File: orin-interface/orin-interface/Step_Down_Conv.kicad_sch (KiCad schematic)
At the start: 2 parts, among them U1 173950336

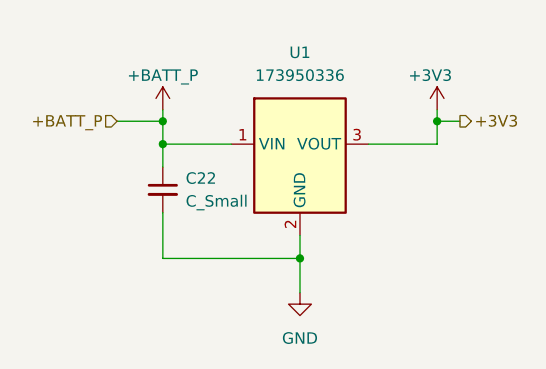
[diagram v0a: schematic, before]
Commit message: orin-interface: PoE channels, buses, 3V3 regulator, ERC fixes
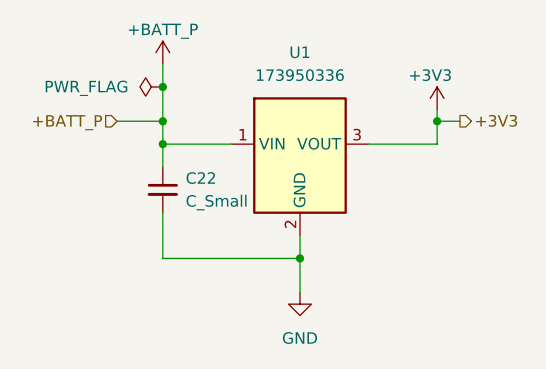
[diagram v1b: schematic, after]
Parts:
- C22: footprint (none) -> Capacitor_SMD:C_0603_1608Metric_Pad1.08x0.95mm_HandSolder
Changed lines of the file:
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@@
+	)
+	(junction
+		(at 134.62 77.47)
+		(diameter 0)
+		(color 0 0 0 0)
 	)
 	(junction
@@
 	(wire
 		(pts
+			(xy 134.62 77.47) (xy 134.62 81.28)
+		)
+		(stroke
+			(width 0)
+			(type default)
+		)
+	)
+	(wire
+		(pts
 			(xy 134.62 83.82) (xy 142.24 83.82)
 		)
@@
 	(wire
 		(pts
-			(xy 134.62 80.01) (xy 134.62 81.28)
+			(xy 134.62 74.93) (xy 134.62 77.47)
 		)
 		(stroke
@@
 	)
 	(symbol
+		(lib_id "power:PWR_FLAG")
+		(at 134.62 77.47 90)
+		(unit 1)
+		(body_style 1)
+		(exclude_from_sim no)
+		(in_bom yes)
+		(on_board yes)
+		(in_pos_files yes)
+		(dnp no)
+		(fields_autoplaced yes)
+		(property "Reference" "#FLG02"
+			(at 132.715 77.47 0)
+			(hide yes)
+			(show_name no)
+			(do_not_autoplace no)
+			(effects
+				(font
+					(size 1.27 1.27)
+				)
+			)
+		)
+		(property "Value" "PWR_FLAG"
+			(at 130.81 77.4699 90)
+			(show_name no)
+			(do_not_autoplace no)
+			(effects
+				(font
+					(size 1.27 1.27)
+				)
+				(justify left)
+			)
+		)
+		(property "Footprint" ""
+			(at 134.62 77.47 0)
+			(hide yes)
+			(show_name no)
+			(do_not_autoplace no)
+			(effects
+				(font
+					(size 1.27 1.27)
+				)
+			)
+		)
+		(property "Datasheet" ""
+			(at 134.62 77.47 0)
+			(hide yes)
+			(show_name no)
+			(do_not_autoplace no)
+			(effects
+				(font
+					(size 1.27 1.27)
+				)
+			)
+		)
+		(property "Description" "Special symbol for telling ERC where power comes from"
+			(at 134.62 77.47 0)
+			(hide yes)
+			(show_name no)
+			(do_not_autoplace no)
+			(effects
+				(font
+					(size 1.27 1.27)
+				)
+			)
+		)
+		(pin "1"
+		)
+		(instances
+			(project "orin-interface"
+				(path "/18aef7c7-2f0e-4a2c-9e5d-7b655e80b6a3/be0ca79a-104a-45dc-920c-2d31e103c726"
+					(reference "#FLG02")
+					(unit 1)
+				)
+			)
+		)
+	)
+	(symbol
 		(lib_id "power:GND")
 		(at 149.86 100.33 0)
@@
 	(symbol
 		(lib_id "power:+BATT")
-		(at 134.62 80.01 0)
+		(at 134.62 74.93 0)
 		(unit 1)
 		(body_style 1)
@@
 		(dnp no)
 		(property "Reference" "#PWR040"
-			(at 134.62 83.82 0)
+			(at 134.62 78.74 0)
 			(hide yes)
 			(show_name no)
@@
 		)
 		(property "Value" "+BATT_P"
-			(at 134.62 76.2 0)
+			(at 134.62 71.12 0)
 			(show_name no)
 			(do_not_autoplace no)
@@
 		)
 		(property "Footprint" ""
-			(at 134.62 80.01 0)
+			(at 134.62 74.93 0)
 			(hide yes)
 			(show_name no)
@@
 		)
 		(property "Datasheet" ""
-			(at 134.62 80.01 0)
+			(at 134.62 74.93 0)
 			(hide yes)
 			(show_name no)
@@
 		)
 		(property "Description" "Power symbol creates a global label with name \"+BATT\""
-			(at 134.62 80.01 0)
+			(at 134.62 74.93 0)
 			(hide yes)
 			(show_name no)
@@
 			)
 		)
-		(property "Footprint" ""
+		(property "Footprint" "Capacitor_SMD:C_0603_1608Metric_Pad1.08x0.95mm_HandSolder"
 			(at 134.62 88.9 0)
 			(hide yes)
